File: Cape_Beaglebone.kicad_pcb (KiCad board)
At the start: 2 copper layers, 54.6 x 86.4 mm, 2 parts, among them P8 BeagleBone_Black_Header, P9 BeagleBone_Black_Header

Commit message: mfsb_29_07_18
Primeira tentativa do layout
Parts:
- added C1, C13, C24: 10n, Capacitors_SMD:C_0805, B.Cu at (157.0, 152.6)
- added C10, C11, C12, C29, C9: C, Capacitors_SMD:C_0805, B.Cu at (157.0, 152.6)
- added C14, C16, C20, C3, C4, C5, C7, C8: 0.1u, Capacitors_SMD:C_0805, B.Cu at (157.0, 152.6)
- added C15, C2, C25, C27, C6: 10u, Capacitors_SMD:C_0805, B.Cu at (157.0, 152.6)
- added C17: 22u, Capacitors_SMD:C_0805, B.Cu at (157.0, 152.6)
- added C18, C26: 4.7u, Capacitors_SMD:C_0805, B.Cu at (157.0, 152.6)
- added C19, C22, C23: 100n, Capacitors_SMD:C_0805, B.Cu at (157.0, 152.6)
- added C21: 0.22u, Capacitors_SMD:C_0805, B.Cu at (157.0, 152.6)
- added C28: 1u, Capacitors_SMD:C_0805, B.Cu at (157.0, 152.6)
- added IC1: MPU-9250, MPU-9250:QFN40P300X300X105-25N-D, B.Cu at (103.7, 157.6)
- added IC10: ADS8688IDBT, ADS8688IDBT:SOP50P640X120-38N, B.Cu at (125.3, 139.9)
- added IC2: HX711, HX711:SOIC127P600X160-16N, B.Cu at (113.8, 152.6)
- added IC3: HX711, HX711:SOIC127P600X160-16N, B.Cu at (125.3, 151.9)
- added IC4: CAT24C256WI-GT3, CAT24C256WI-GT3:SOIC127P800X203-8N, B.Cu at (113.8, 138.6)
- added IC5: AD7793BRUZ, AD7793BRUZ:SOP65P640X120-16N, B.Cu at (102.4, 138.6)
- added IC6: AD7793BRUZ, AD7793BRUZ:SOP65P640X120-16N, B.Cu at (91.0, 138.6)
- added IC7: MPU-6500, MPU-6500:QFN40P300X300X95-25N-D, B.Cu at (111.3, 152.6)
- added IC8: HMC5883L-TR, HMC5883L-TR:16-PIN-LPCC, B.Cu at (89.7, 157.6)
- added IC9: BMP180, BMP180:BMP180, B.Cu at (110.0, 146.2)
- added J1: Conn_01x04, Connectors_JST:JST_GH_BM04B-GHS-TBT_04x1.25mm_Straight, F.Cu at (179.2, 80.2)
- added J10: Conn_01x12, Connectors_JST:JST_GH_BM12B-GHS-TBT_12x1.25mm_Straight, F.Cu at (198.9, 81.4)
- added J11: Conn_01x08, Connectors_JST:JST_GH_BM08B-GHS-TBT_08x1.25mm_Straight, F.Cu at (196.4, 110.6)
- added J12: Conn_01x08, Connectors_JST:JST_GH_BM08B-GHS-TBT_08x1.25mm_Straight, F.Cu at (196.4, 120.8)
- added J2: Conn_01x02, Connectors_JST:JST_GH_BM02B-GHS-TBT_02x1.25mm_Straight, F.Cu at (179.9, 71.3)
- added J3: Conn_01x04, Connectors_JST:JST_GH_BM04B-GHS-TBT_04x1.25mm_Straight, F.Cu at (179.2, 89.1)
- added J4: Conn_01x04, Connectors_JST:JST_GH_BM04B-GHS-TBT_04x1.25mm_Straight, F.Cu at (179.2, 97.9)
- added J6: Conn_01x12, Connectors_JST:JST_GH_BM12B-GHS-TBT_12x1.25mm_Straight, F.Cu at (198.9, 72.5)
- added J7: Conn_01x04, Connectors_JST:JST_GH_BM04B-GHS-TBT_04x1.25mm_Straight, F.Cu at (179.2, 106.8)
- added J8: Conn_01x08, Connectors_JST:JST_GH_BM08B-GHS-TBT_08x1.25mm_Straight, F.Cu at (196.4, 91.6)
- added J9: Conn_01x08, Connectors_JST:JST_GH_BM08B-GHS-TBT_08x1.25mm_Straight, F.Cu at (196.4, 100.5)
- added Q1: BC807, TO_SOT_Packages_SMD:SOT-23, B.Cu at (97.3, 146.2)
- added Q2: BC807, TO_SOT_Packages_SMD:SOT-23, B.Cu at (97.3, 152.6)
- added R1, R2, R3: R, Resistors_SMD:R_0805, B.Cu at (157.0, 152.6)
- added R10, R11, R12, R13, R14: 10k, Resistors_SMD:R_0805, B.Cu at (157.0, 152.1)
- added R4, R5, R6: R, Resistors_SMD:R_0805, B.Cu at (157.0, 152.1)
- added R7, R8, R9: 4.7k, Resistors_SMD:R_0805, B.Cu at (157.0, 152.1)
- added U1: DS3231S#, DS3231S#:SOIC127P1032X265-16N, B.Cu at (136.4, 97.4)
- added U2: 4525DO-DS5AI001DP, 4525DO-DS5AI001DP:4525DO-DS...P, F.Cu at (148.9, 125.4)
- added U3: LSM303D, LSM303DLHC:LGA14-3X5X1-14L, B.Cu at (120.2, 144.9)
- added U4: L3GD20, L3GD20TR:L3GD20TR, B.Cu at (103.7, 146.2)
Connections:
- net GNDD renamed -BATT
- net Net-(P8-Pad13) renamed INTERUP_SEN_7a
- net Net-(P8-Pad15) renamed INTERUP_SEN_7b
- P8 pad 10: Net-(P8-Pad10) -> INTERUP_SEN_4
- P8 pad 11: Net-(P8-Pad11) -> INTERUP_SEN_5
- P8 pad 14: Net-(P8-Pad14) -> INTERUP_SEN_8a
- P8 pad 16: Net-(P8-Pad16) -> INTERUP_SEN_8b
- P8 pad 7: Net-(P8-Pad7) -> INTERUP_SEN_1
- P8 pad 8: Net-(P8-Pad8) -> INTERUP_SEN_2
- P9 pad 17: Net-(P9-Pad17) -> SCL_I2C_1
- P9 pad 18: Net-(P9-Pad18) -> SDA_I2C_1
- P9 pad 19: Net-(P9-Pad19) -> SCL_I2C_2
- P9 pad 20: Net-(P9-Pad20) -> SDA_I2C_2
- P9 pad 29: Net-(P9-Pad29) -> SPI_SD0
- P9 pad 30: Net-(P9-Pad30) -> SPI_SDI
- P9 pad 31: Net-(P9-Pad31) -> SPI_SPC
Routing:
- added copper zone on B.Cu, net +3V3
- added copper zone on F.Cu, net GNDD

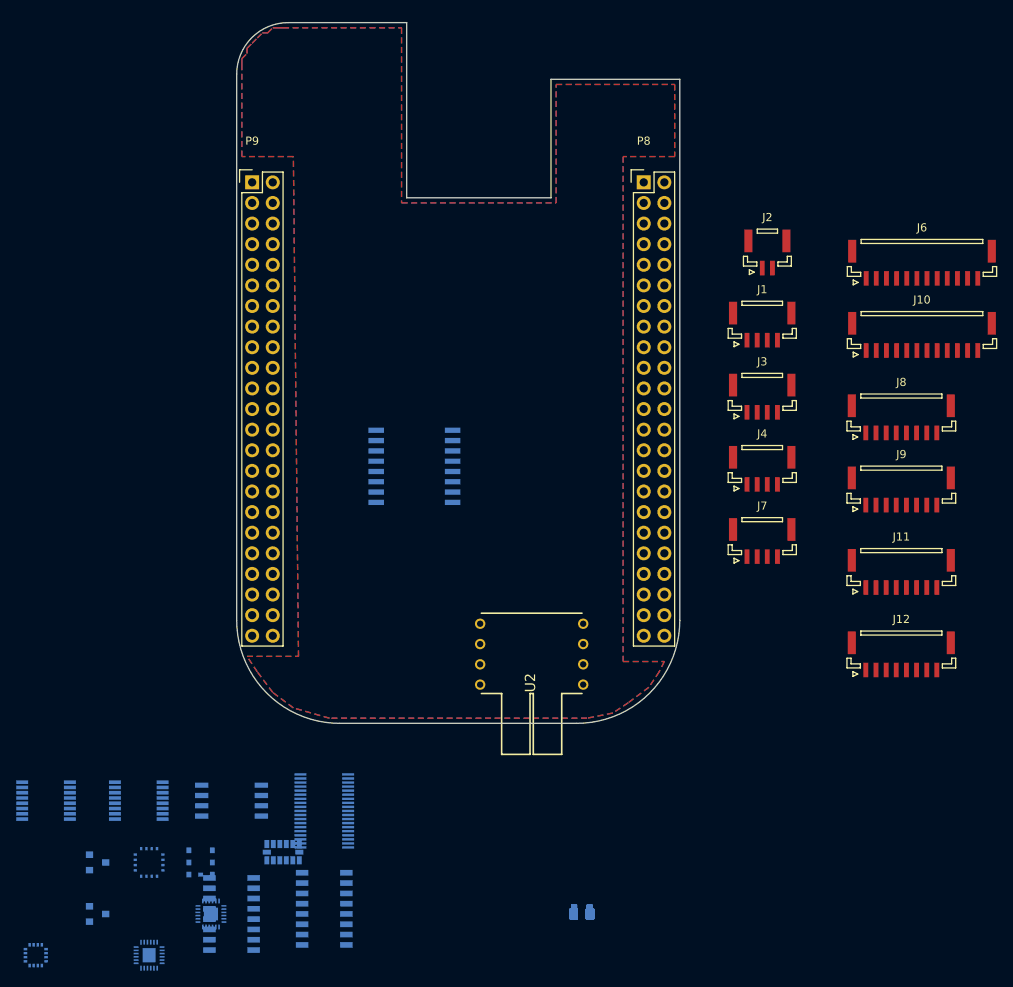
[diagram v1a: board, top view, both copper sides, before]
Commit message: Layout com SJT GH
Layout quase finalizado usando os conectores SJT GH de 1,25 mm
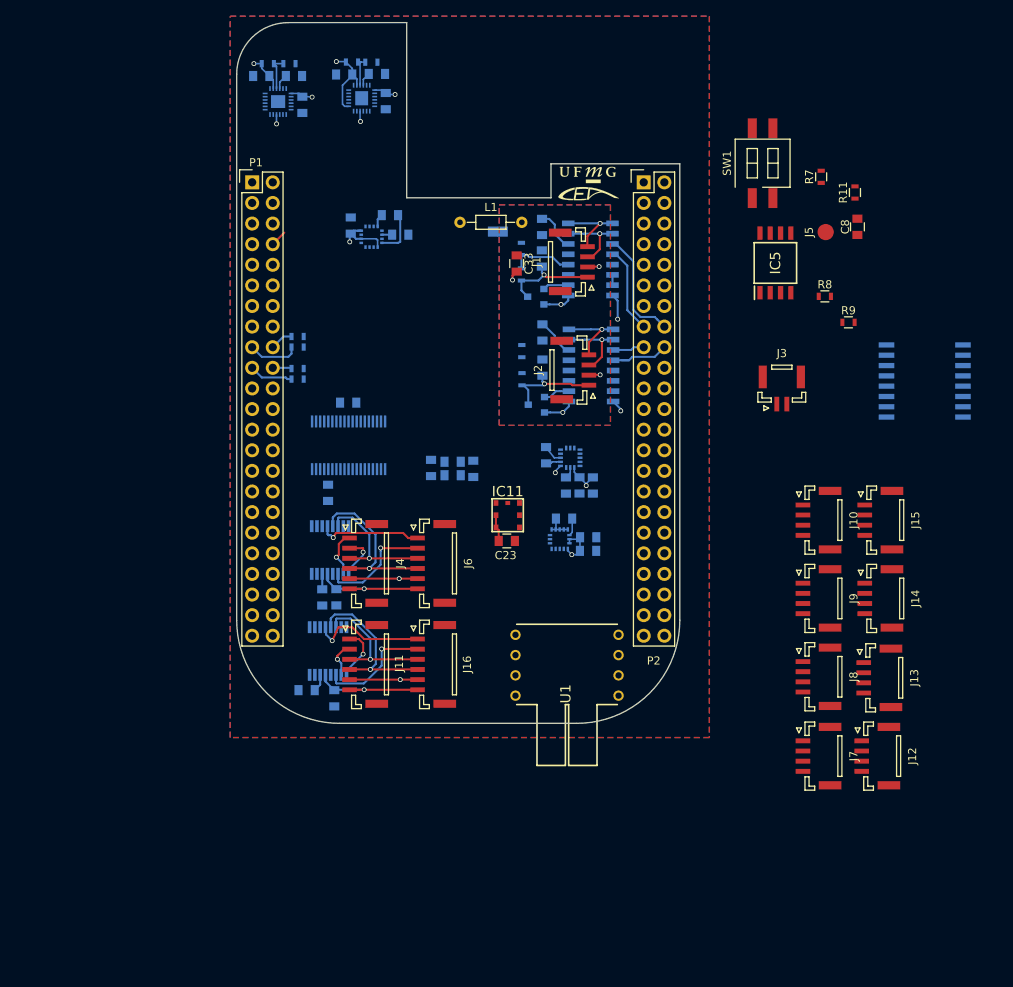
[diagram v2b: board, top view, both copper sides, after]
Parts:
- removed P8, P9: BeagleBone_Black_Header, Socket_BeagleBone_Black:Socket_BeagleBone_Black
- removed U2: 4525DO-DS5AI001DP, 4525DO-DS5AI001DP:4525DO-DS...P
- removed U3: LSM303D, LSM303DLHC:LGA14-3X5X1-14L
- removed U4: L3GD20, L3GD20TR:L3GD20TR
- added C30: 1u, Capacitors_SMD:C_0805, B.Cu at (128.2, 89.5)
- added C31: 10n, Capacitors_SMD:C_0805, B.Cu at (154.8, 103.8)
- added C32: 10u, Capacitors_SMD:C_0805, B.Cu at (157.8, 107.8)
- added C33: C, Capacitors_SMD:C_0805, F.Cu at (149.0, 72.4)
- added G***: UFMG, complementos:UFMG, F.Cu at (157.7, 61.5)
- added G***: CEA, complementos:CEA, F.Cu at (157.8, 63.8)
- added IC11: BMP180, BMP180:BMP180, F.Cu at (147.9, 103.4)
- added IC12: ADS8688IDBT, ADS8688IDBT:SOP50P640X120-38N, B.Cu at (128.3, 94.8)
- added IC13: L3GD20H, L3GD20H_CORRETO:LGA(3X3X1.0-16L), B.Cu at (154.3, 106.4)
- added J13: Conn_01x04, Connectors_JST:JST_GH_BM04B-GHS-TBT_04x1.25mm_Straight, F.Cu at (193.4, 123.4)
- added J14: Conn_01x04, Connectors_JST:JST_GH_BM04B-GHS-TBT_04x1.25mm_Straight, F.Cu at (193.5, 113.7)
- added J15: Conn_01x04, Connectors_JST:JST_GH_BM04B-GHS-TBT_04x1.25mm_Straight, F.Cu at (193.5, 104.0)
- added J16: Conn_01x06, Connectors_JST:JST_GH_BM06B-GHS-TBT_06x1.25mm_Straight, F.Cu at (138.4, 121.8)
- added J5: M_WP, complemento2:test_pad, F.Cu at (184.5, 68.5)
- added L1: I, Resistors_THT:R_Axial_DIN0204_L3.6mm_D1.6mm_P7.62mm_Horizontal, F.Cu at (142.0, 67.3)
- added NT1: Net-Tie_2, complementos:net_tie2, B.Cu at (144.7, 69.7)
- added P1: BeagleBone_Black_Header, Socket_BeagleBone_Black:Socket_BeagleBone_Black, F.Cu at (116.4, 62.4)
- added P2: BeagleBone_Black_Header, Socket_BeagleBone_Black:Socket_BeagleBone_Black, F.Cu at (164.6, 62.4)
- added R15: 10k, Resistors_SMD:R_0603, B.Cu at (122.0, 82.7)
- added R16: 10k, Resistors_SMD:R_0603, B.Cu at (122.0, 81.4)
- added SW1: SW_DIP_x02, Buttons_Switches_SMD:SW_DIP_x2_W8.61mm_Slide_LowProfile, F.Cu at (179.3, 60.0)
- C1: value 10n -> 10u
- C13: value 10n -> C
- C14: value 0.1u -> 10n
- C15: value 10u -> 0.1u
- C17: value 22u -> 4.7u
- C18: value 4.7u -> 10u
- C19: value 100n -> 0.1u
- C2: value 10u -> 10n
- C20: value 0.1u -> 1u
- C23, C8: moved to F.Cu
- C24: value 10n -> 22u
- C26: value 4.7u -> 1u
- C27: value 10u -> 4.7u
- C28: value 1u -> 100n
- C29: value C -> 10u
- C9: value C -> 22u
- IC10: value ADS8688IDBT -> HMC5883L-TR; footprint ADS8688IDBT:SOP50P640X120-38N -> HMC5883L-TR:16-PIN-LPCC
- IC3: value HX711 -> DS3231S; footprint HX711:SOIC127P600X160-16N -> DS3231S#:SOIC127P1032X265-16N
- IC4: value CAT24C256WI-GT3 -> HX711; footprint CAT24C256WI-GT3:SOIC127P800X203-8N -> HX711:SOIC127P600X160-16N
- IC5: value AD7793BRUZ -> CAT24C256WI-GT3; footprint AD7793BRUZ:SOP65P640X120-16N -> CAT24C256WI-GT3:SOIC127P800X203-8N; moved to F.Cu
- IC7: value MPU-6500 -> AD7793BRUZ; footprint MPU-6500:QFN40P300X300X95-25N-D -> AD7793BRUZ:SOP65P640X120-16N
- IC8: value HMC5883L-TR -> MPU-6500; footprint HMC5883L-TR:16-PIN-LPCC -> MPU-6500:QFN40P300X300X95-25N-D
- IC9: value BMP180 -> LSM303D; footprint BMP180:BMP180 -> LSM303D:PQFN50P300X300X100-16N
- J10: value Conn_01x12 -> Conn_01x04; footprint Connectors_JST:JST_GH_BM12B-GHS-TBT_12x1.25mm_Straight -> Connectors_JST:JST_GH_BM04B-GHS-TBT_04x1.25mm_Straight
- J11: value Conn_01x08 -> Conn_01x06; footprint Connectors_JST:JST_GH_BM08B-GHS-TBT_08x1.25mm_Straight -> Connectors_JST:JST_GH_BM06B-GHS-TBT_06x1.25mm_Straight
- J12, J8, J9: value Conn_01x08 -> Conn_01x04; footprint Connectors_JST:JST_GH_BM08B-GHS-TBT_08x1.25mm_Straight -> Connectors_JST:JST_GH_BM04B-GHS-TBT_04x1.25mm_Straight
- J2: value Conn_01x02 -> Conn_01x04; footprint Connectors_JST:JST_GH_BM02B-GHS-TBT_02x1.25mm_Straight -> Connectors_JST:JST_GH_BM04B-GHS-TBT_04x1.25mm_Straight
- J3: value Conn_01x04 -> Conn_01x02; footprint Connectors_JST:JST_GH_BM04B-GHS-TBT_04x1.25mm_Straight -> Connectors_JST:JST_GH_BM02B-GHS-TBT_02x1.25mm_Straight
- J4: value Conn_01x04 -> Conn_01x06; footprint Connectors_JST:JST_GH_BM04B-GHS-TBT_04x1.25mm_Straight -> Connectors_JST:JST_GH_BM06B-GHS-TBT_06x1.25mm_Straight
- J6: value Conn_01x12 -> Conn_01x06; footprint Connectors_JST:JST_GH_BM12B-GHS-TBT_12x1.25mm_Straight -> Connectors_JST:JST_GH_BM06B-GHS-TBT_06x1.25mm_Straight
- R1, R10, R12, R2, R3, R4, R5, R6: footprint Resistors_SMD:R_0805 -> Resistors_SMD:R_0603
- R11, R7, R8, R9: footprint Resistors_SMD:R_0805 -> Resistors_SMD:R_0603; moved to F.Cu
- R13, R14: value 10k -> R; footprint Resistors_SMD:R_0805 -> Resistors_SMD:R_0603
- U1: value DS3231S# -> 4525DO-DS5AI001DP; footprint DS3231S#:SOIC127P1032X265-16N -> 4525DO-DS5AI001DP:4525DO-DS...P; moved to F.Cu
- moved R13 111.3 mm to (118.3, 47.8), turned to 180 degrees
- moved C14 110.6 mm to (117.5, 49.3), turned to 180 degrees
- moved R14 110.4 mm to (121.0, 47.8), turned to 180 degrees
- moved IC8 109.4 mm to (119.6, 52.4)
- moved C15 109.2 mm to (121.5, 49.3), turned to 180 degrees
- moved IC1 108.8 mm to (129.9, 52.0)
- moved R3 108.7 mm to (128.7, 47.6), turned to 180 degrees
- moved R4 107.7 mm to (131.1, 47.6), turned to 180 degrees
- moved C2 107.5 mm to (127.7, 49.1), turned to 180 degrees
- moved C4 106.6 mm to (131.7, 49.0), turned to 180 degrees
- moved C16 105.5 mm to (122.6, 52.8), turned to 270 degrees
- moved C5 103.1 mm to (132.8, 52.4), turned to 270 degrees
- moved IC5 102.7 mm to (180.9, 72.3), turned to 90 degrees
- moved IC3 98.5 mm to (199.3, 86.9), turned to 180 degrees
- moved R7 95.1 mm to (186.5, 61.7), turned to 90 degrees
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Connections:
- C1 pad 1: +3V3 -> GNDA
- C1 pad 2: -BATT -> Net-(C1-Pad2)
- C10 pad 1: +5VA -> GNDD
- C10 pad 2: GNDA -> +3V3
- C11 pad 1: GND -> +5VA
- C11 pad 2: +3V3 -> GNDA
- C12 pad 1: +5VA -> GNDD
- C12 pad 2: GNDA -> +3V3
- C13 pad 1: +3V3 -> +5VA
- C13 pad 2: -BATT -> GNDA
- C14 pad 1: Net-(C14-Pad1) -> +3V3
- C14 pad 2: -BATT -> GNDD
- C15 pad 1: +3V3 -> GNDD
- C15 pad 2: -BATT -> Net-(C15-Pad2)
- C16 pad 2: -BATT -> GNDD
- C17 pad 2: Net-(C17-Pad2) -> GNDD
- C18 pad 1: Net-(C18-Pad1) -> +3V3
- C18 pad 2: -BATT -> GNDD
- C19 pad 2: -BATT -> GNDD
- C2 pad 1: GNDA -> +3V3
- C2 pad 2: +5VA -> GNDD
- C20 pad 1: +3V3 -> +5VA
- C20 pad 2: -BATT -> GNDA
- C22 pad 2: Net-(C22-Pad2) -> GNDD
- C23 pad 2: -BATT -> GNDD
- C24 pad 2: -BATT -> GNDA
- C25 pad 1: +3V3 -> GNDA
- C25 pad 2: -BATT -> Net-(C25-Pad2)
- C26 pad 1: -BATT -> Net-(C24-Pad1)
- C26 pad 2: Net-(C26-Pad2) -> GNDA
- C27 pad 1: +3V3 -> GNDD
- C27 pad 2: -BATT -> Net-(C27-Pad2)
- C28 pad 1: GNDA -> +3V3
- C28 pad 2: +5VA -> GNDD
- C29 pad 1: +5VA -> +3V3
- C29 pad 2: GNDA -> GNDD
- C4 pad 1: -BATT -> GNDD
- C5 pad 2: -BATT -> GNDD
- C6 pad 2: +5VA -> Net-(C6-Pad2)
- C8 pad 2: -BATT -> GNDD
- C9 pad 1: GND -> Net-(C9-Pad1)
- C9 pad 2: +3V3 -> Net-(C9-Pad2)
- IC1 pad 12: INTERUP_SEN_4 -> INTERUP_SEN_3
- IC1 pad 18: -BATT -> GNDD
- IC1 pad 20: -BATT -> GNDD
- IC1 pad 25: Net-(IC1-Pad25) -> GNDD
- IC10 pad 1: SPI_SDI -> SCL_I2C_1
- IC10 pad 10: Net-(IC10-Pad10) -> Net-(C27-Pad2)
- IC10 pad 11: Net-(IC10-Pad11) -> GNDD
- IC10 pad 12: /AIN_6P -> Net-(C21-Pad2)
- IC10 pad 13: /AIN_6N -> +3V3
- IC10 pad 14: /AIN_7P -> Net-(IC10-Pad14)
- IC10 pad 15: /AIN_7N -> INTERUP_SEN_2
- IC10 pad 16: /AIN_0P -> SDA_I2C_1
- IC10 pad 2: Net-(IC10-Pad2) -> +3V3
- IC10 pad 4: Net-(IC10-Pad4) -> +3V3
- IC10 pad 8: GNDA -> Net-(C21-Pad1)
- IC10 pad 9: +5VA -> GNDD
- IC2 pad 1: Net-(IC2-Pad1) -> +5VA
- IC2 pad 11: Net-(IC2-Pad11) -> HX1_SCK
- IC2 pad 12: Net-(IC2-Pad12) -> HX1_DOUT
- IC2 pad 14: -BATT -> GNDD
- IC2 pad 15: -BATT -> GNDD
- IC2 pad 7: Net-(IC2-Pad7) -> Net-(IC2-Pad10)
- IC2 pad 9: Net-(IC2-Pad9) -> Net-(IC2-Pad8)
- IC3 pad 10: Net-(IC3-Pad10) -> GNDD
- IC3 pad 11: Net-(IC3-Pad11) -> GNDD
- IC3 pad 12: Net-(IC3-Pad12) -> GNDD
- IC3 pad 13: Net-(IC3-Pad13) -> GNDD
- IC3 pad 14: -BATT -> Net-(IC3-Pad14)
- IC3 pad 15: -BATT -> SDA_I2C_2
- IC3 pad 16: +3V3 -> SCL_I2C_2
- IC3 pad 2: Net-(IC3-Pad2) -> +3V3
- IC3 pad 3: +5VA -> INTERUP_RTC
- IC3 pad 5: GNDA -> GNDD
- IC3 pad 6: Net-(C7-Pad1) -> GNDD
- IC3 pad 7: Net-(IC3-Pad7) -> GNDD
- IC3 pad 8: Net-(IC3-Pad8) -> GNDD
- IC3 pad 9: Net-(IC3-Pad9) -> GNDD
- IC4 pad 1: Net-(IC4-Pad1) -> +5VA
- IC4 pad 3: Net-(IC4-Pad3) -> +5VA
- IC4 pad 4: -BATT -> Net-(IC4-Pad4)
- IC4 pad 5: SDA_I2C_2 -> GNDA
- IC4 pad 6: SCL_I2C_2 -> Net-(C7-Pad1)
- IC4 pad 7: Net-(IC4-Pad7) -> Net-(IC4-Pad10)
- IC4 pad 8: +3V3 -> Net-(IC4-Pad8)
- IC5 pad 1: SPI_SPC -> Net-(IC5-Pad1)
- IC5 pad 3: SPI_CS_S1 -> Net-(IC5-Pad3)
- IC5 pad 4: Net-(IC5-Pad4) -> GNDD
- IC5 pad 5: /AIN_8P -> SDA_I2C_2
- IC5 pad 6: /AIN_8N -> SCL_I2C_2
- IC5 pad 7: /AIN_9P -> Net-(IC5-Pad7)
- IC5 pad 8: /AIN_9N -> +3V3
- IC6 pad 11: Net-(IC6-Pad11) -> /IOUT_4
- IC6 pad 4: Net-(IC6-Pad4) -> /IOUT_3
- IC6 pad 7: /AIN_12P -> Net-(IC6-Pad7)
- IC6 pad 8: /AIN_12N -> Net-(IC6-Pad8)
- IC7 pad 1: Net-(IC7-Pad1) -> SPI_SPC
- IC7 pad 10: Net-(C14-Pad1) -> /AIN_9P
- IC7 pad 11: Net-(IC7-Pad11) -> /IOUT_2
- IC7 pad 12: INTERUP_SEN_1 -> GNDA
- IC7 pad 13: +3V3 -> +5VA
- IC7 pad 14: Net-(IC7-Pad14) -> +3V3
- IC7 pad 15: Net-(IC7-Pad15) -> SPI_SD0
- IC7 pad 16: Net-(IC7-Pad16) -> SPI_SDI
- IC7 pad 3: Net-(IC7-Pad3) -> SPI_CS_S1
- IC7 pad 4: Net-(IC7-Pad4) -> /IOUT_1
- IC7 pad 5: Net-(IC7-Pad5) -> /AIN_8P
- IC7 pad 6: Net-(IC7-Pad6) -> /AIN_8N
- IC7 pad 8: +3V3 -> Net-(IC7-Pad8)
- IC7 pad 9: Net-(IC7-Pad9) -> /AIN_9N
- IC8 pad 1: SCL_I2C_1 -> Net-(IC8-Pad1)
- IC8 pad 10: Net-(C26-Pad2) -> Net-(C15-Pad2)
- IC8 pad 11: -BATT -> Net-(IC8-Pad11)
- IC8 pad 12: Net-(C21-Pad2) -> INTERUP_SEN_1
- IC8 pad 15: INTERUP_SEN_2 -> Net-(IC8-Pad15)
- IC8 pad 16: SDA_I2C_1 -> Net-(IC8-Pad16)
- IC8 pad 2: +3V3 -> Net-(IC8-Pad2)
- IC8 pad 4: +3V3 -> Net-(IC8-Pad4)
- IC8 pad 8: Net-(C21-Pad1) -> +3V3
- IC8 pad 9: -BATT -> Net-(IC8-Pad9)
- IC9 pad 1: Net-(IC9-Pad1) -> +3V3
- IC9 pad 2: +3V3 -> Net-(C9-Pad1)
- IC9 pad 3: +3V3 -> Net-(C9-Pad2)
- IC9 pad 4: Net-(IC9-Pad4) -> SPI_SPC
- IC9 pad 5: SCL_I2C_1 -> GNDD
- IC9 pad 6: SDA_I2C_1 -> SPI_SDI
- IC9 pad 7: -BATT -> SPI_SD0
- J1 pad 1: +5VA -> Net-(C1-Pad2)
- J1 pad 3: Net-(IC2-Pad8) -> Net-(IC2-Pad10)
- J1 pad 4: Net-(IC2-Pad7) -> Net-(IC2-Pad8)
- J10 pad 1: /AIN_11P -> GNDA
- J10 pad 2: /AIN_11N -> +5VA
- J10 pad 3: +5VA -> /AIN_1P
- J10 pad 4: GNDA -> /AIN_1N
- J11 pad 1: /AIN_4N -> /AIN_13P
- J11 pad 2: /AIN_4P -> /AIN_13N
- J11 pad 3: +5VA -> /AIN_11N
- J11 pad 4: GNDA -> /AIN_11P
- J11 pad 5: /AIN_5N -> GNDA
- J11 pad 6: /AIN_5P -> +5VA
- J12 pad 1: /AIN_2N -> GNDA
- J12 pad 2: /AIN_2P -> +5VA
- J12 pad 3: +5VA -> /AIN_5P
- J12 pad 4: GNDA -> /AIN_5N
- J2 pad 1: -BATT -> Net-(C6-Pad2)
- J2 pad 2: +BATT -> GNDA
- J3 pad 1: +5VA -> Net-(IC3-Pad14)
- J3 pad 2: GNDA -> GNDD
- J4 pad 1: +5VA -> /AIN_9P
- J4 pad 2: GNDA -> /AIN_9N
- J4 pad 3: Net-(IC3-Pad8) -> /AIN_8N
- J4 pad 4: Net-(IC3-Pad7) -> /AIN_8P
- J6 pad 1: /AIN_8P -> /IOUT_1
- J6 pad 2: /AIN_8N -> /IOUT_2
- J6 pad 3: +5VA -> /AIN_8N
- J6 pad 4: GNDA -> /AIN_8P
- J6 pad 5: /AIN_9P -> GNDA
- J6 pad 6: /AIN_9N -> +5VA
- J7 pad 1: +5VA -> GNDA
- J7 pad 2: GNDA -> +5VA
- J7 pad 3: Net-(IC3-Pad9) -> /AIN_6P
- J7 pad 4: Net-(IC3-Pad10) -> /AIN_6N
- J8 pad 1: /AIN_7N -> GNDA
- J8 pad 2: /AIN_7P -> +5VA
- J8 pad 3: +5VA -> /AIN_7P
- J8 pad 4: GNDA -> /AIN_7N
- J9 pad 1: /AIN_1N -> GNDA
- J9 pad 2: /AIN_1P -> +5VA
- J9 pad 3: +5VA -> /AIN_0P
- J9 pad 4: GNDA -> /AIN_0N
- Q1 pad 2: Net-(IC2-Pad1) -> +5VA
- Q1 pad 3: +5VA -> Net-(C1-Pad2)
- Q2 pad 1: Net-(IC3-Pad2) -> Net-(IC4-Pad2)
- Q2 pad 2: Net-(IC3-Pad1) -> +5VA
- Q2 pad 3: +5VA -> Net-(C6-Pad2)
- R1 pad 1: Net-(IC1-Pad9) -> Net-(IC2-Pad4)
- R1 pad 2: +3V3 -> Net-(C1-Pad2)
- R11 pad 2: Net-(IC4-Pad7) -> Net-(IC5-Pad7)
- R13 pad 1: SCL_I2C_1 -> Net-(IC8-Pad9)
- R14 pad 1: SDA_I2C_1 -> GNDD
- R14 pad 2: +3V3 -> Net-(IC8-Pad9)
- R2 pad 1: +5VA -> GNDA
- R3 pad 1: Net-(IC2-Pad4) -> Net-(IC1-Pad9)
- R3 pad 2: GNDA -> +3V3
- R4 pad 1: -BATT -> GNDD
- R5 pad 1: +5VA -> Net-(IC4-Pad4)
- R5 pad 2: Net-(IC3-Pad4) -> Net-(C6-Pad2)
- R6 pad 1: Net-(IC3-Pad4) -> GNDA
- R6 pad 2: GNDA -> Net-(IC4-Pad4)
- R7 pad 2: Net-(IC4-Pad1) -> Net-(IC5-Pad1)
- R8 pad 2: Net-(IC4-Pad2) -> Net-(IC5-Pad2)
- R9 pad 2: Net-(IC4-Pad3) -> Net-(IC5-Pad3)
- U1 pad 1: Net-(U1-Pad1) -> GNDD
- U1 pad 3: Net-(U1-Pad3) -> SDA_I2C_2
- U1 pad 4: Net-(SW1-Pad4) -> SCL_I2C_2
- U1 pad 5: -BATT -> INTERUP_SEN_4
- U1 pad 6: -BATT -> Net-(U1-Pad6)
- U1 pad 7: -BATT -> Net-(U1-Pad7)
- U1 pad 8: -BATT -> Net-(U1-Pad8)
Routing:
- net +3V3: track 0.00 -> 53.3 mm, vias 0 -> 12
- net +5VA: track 0.00 -> 36.3 mm, vias 0 -> 4
- net GNDA: track 0.00 -> 20.9 mm, vias 0 -> 5
- net /AIN_11P: track 0.00 -> 20.6 mm, vias 0 -> 1
- net /AIN_8P: track 0.00 -> 20.5 mm, vias 0 -> 1
- net /AIN_11N: track 0.00 -> 17.2 mm, vias 0 -> 1
- net /AIN_8N: track 0.00 -> 17.1 mm, vias 0 -> 1
- net /IOUT_3: track 0.00 -> 14.2 mm, vias 0 -> 1
- net HX1_SCK: track 0.00 -> 14.1 mm
- net /IOUT_4: track 0.00 -> 14.0 mm, vias 0 -> 1
- net /IOUT_2: track 0.00 -> 13.8 mm, vias 0 -> 1
- net /IOUT_1: track 0.00 -> 12.9 mm, vias 0 -> 1
- net Net-(C6-Pad2): track 0.00 -> 12.3 mm, vias 0 -> 1
- net Net-(C1-Pad2): track 0.00 -> 12.0 mm, vias 0 -> 1
- net HX1_DOUT: track 0.00 -> 10.8 mm
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- added copper zone on F.Cu, net +3V3
- added copper zone on F.Cu, net +5VA
- added copper zone on B.Cu, net GNDA
- added copper zone on B.Cu, net GNDD
- removed copper zone on B.Cu, net +3V3
- removed copper zone on F.Cu, net GNDD
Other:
- outline, holes or cut-outs redrawn
- net class fina added: clearance 0.15, trace_width 0.2, via_dia 0.6, via_drill 0.4

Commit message: Final V1.0
Primeria versão final sem revisão
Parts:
- removed the G*** at (157.7, 61.5)
- removed the G*** at (157.8, 63.8)
- added C34: C, Capacitors_SMD:C_0805, F.Cu at (138.5, 67.4)
- added G***: LOGO, complementos:LOGO, F.Cu at (122.0, 91.0)
- added L2: I, Resistors_THT:R_Axial_DIN0204_L3.6mm_D1.6mm_P7.62mm_Horizontal, F.Cu at (133.5, 74.6)
- added NT2: Net-Tie_2, complementos:net_tie2, B.Cu at (136.2, 71.4)
- added R17: 0, Resistors_SMD:R_0603, F.Cu at (166.7, 57.9)
- added R18: 0, Resistors_SMD:R_0603, F.Cu at (165.5, 57.9)
- C17, C18, C22, C9, IC9, R10, R12, R15, R16: moved to F.Cu
- J1, J10, J12, J13, J14, J15, J2, J7, J8, J9: footprint Connectors_JST:JST_GH_BM04B-GHS-TBT_04x1.25mm_Straight -> Connectors_JST:JST_SH_BM04B-SRSS-TB_04x1.00mm_Straight
- J11, J16, J4, J6: footprint Connectors_JST:JST_GH_BM06B-GHS-TBT_06x1.25mm_Straight -> Connectors_JST:JST_SH_BM06B-SRSS-TB_06x1.00mm_Straight
- J3: footprint Connectors_JST:JST_GH_BM02B-GHS-TBT_02x1.25mm_Straight -> Connectors_JST:JST_SH_BM02B-SRSS-TB_02x1.00mm_Straight
- SW1: footprint Buttons_Switches_SMD:SW_DIP_x2_W8.61mm_Slide_LowProfile -> Buttons_Switches_SMD:SW_DIP_x2_W5.08mm_Slide_Copal_CHS-A
- moved C10 75.3 mm to (191.3, 93.2), turned to 90 degrees
- moved C11 75.0 mm to (192.0, 89.6), turned to 90 degrees
- moved U1 72.1 mm to (187.8, 63.4), turned to 180 degrees
- moved IC6 67.6 mm to (186.5, 90.5), turned to 0 degrees
- moved J11 65.2 mm to (184.3, 85.6), turned to 90 degrees
- moved J4 63.9 mm to (184.3, 75.5), turned to 90 degrees
- moved J16 62.9 mm to (189.9, 85.6), turned to 90 degrees
- moved J6 61.6 mm to (189.9, 75.5), turned to 90 degrees
- moved C13 59.9 mm to (181.4, 89.1), turned to 90 degrees
- moved J7 59.2 mm to (152.0, 84.7), turned to 180 degrees
- moved C12 59.1 mm to (180.6, 93.6)
- moved J8 55.8 mm to (152.0, 79.1), turned to 180 degrees
- moved IC7 52.2 mm to (175.3, 90.5), turned to 0 degrees
- moved J12 51.4 mm to (176.1, 84.6), turned to 180 degrees
- moved R13 49.4 mm to (118.5, 97.1), turned to 270 degrees
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- renumbered P1 to P8, P2 to P9
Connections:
- net Net-(P1-Pad32) renamed VDD_ADC
- net Net-(P1-Pad34) renamed GNDA_ADC
- C1 pad 1: GNDA -> GNDA_aux
- C3 pad 2: GNDA -> GNDA_aux
- C6 pad 1: GNDA -> GNDA_aux
- C7 pad 2: GNDA -> GNDA_aux
- IC2 pad 1: +5VA -> +5VA_aux
- IC2 pad 3: +5VA -> +5VA_aux
- IC2 pad 5: GNDA -> GNDA_aux
- IC4 pad 1: +5VA -> +5VA_aux
- IC4 pad 3: +5VA -> +5VA_aux
- IC4 pad 5: GNDA -> GNDA_aux
- J1 pad 2: GNDA -> GNDA_aux
- J11 pad 3: /AIN_11N -> /AIN_11P
- J11 pad 4: /AIN_11P -> /AIN_11N
- J16 pad 1: /IOUT_3 -> /IOUT_4
- J16 pad 2: /IOUT_4 -> /IOUT_3
- J16 pad 3: /AIN_11N -> /AIN_11P
- J16 pad 4: /AIN_11P -> /AIN_11N
- J2 pad 2: GNDA -> GNDA_aux
- J4 pad 3: /AIN_8N -> /AIN_8P
- J4 pad 4: /AIN_8P -> /AIN_8N
- J6 pad 1: /IOUT_1 -> /IOUT_2
- J6 pad 2: /IOUT_2 -> /IOUT_1
- J6 pad 3: /AIN_8N -> /AIN_8P
- J6 pad 4: /AIN_8P -> /AIN_8N
- L1 pad 1: SYS_5V -> +5V
- P8 pad 10: Net-(P1-Pad10) -> INTERUP_SEN_7b
- P8 pad 11: Net-(P1-Pad11) -> SPI_CS_S5
- P8 pad 14: Net-(P1-Pad14) -> SPI_CS_S4
- P8 pad 15: Net-(P1-Pad15) -> INTERUP_SEN_8b
- P8 pad 16: Net-(P1-Pad16) -> INTERUP_SEN_8a
- P8 pad 23: INTERUP_RTC -> Net-(P1-Pad23)
- P8 pad 28: Net-(P1-Pad28) -> SPI_CS_S3
- P8 pad 36: Net-(P1-Pad36) -> SPI_CS_S1
- P8 pad 42: Net-(P1-Pad42) -> SPI_CS_S2
- P8 pad 5: Net-(P1-Pad5) -> +5V
- P8 pad 6: Net-(P1-Pad6) -> +5V
- P8 pad 7: SYS_5V -> INTERUP_SEN_1
- P8 pad 8: SYS_5V -> INTERUP_SEN_2
- P8 pad 9: Net-(P1-Pad9) -> INTERUP_SEN_7a
- P9 pad 10: INTERUP_SEN_4 -> Net-(P2-Pad10)
- P9 pad 11: INTERUP_SEN_7a -> Net-(P2-Pad11)
- P9 pad 12: INTERUP_SEN_8a -> Net-(P2-Pad12)
- P9 pad 13: INTERUP_SEN_7b -> Net-(P2-Pad13)
- P9 pad 14: INTERUP_SEN_8b -> Net-(P2-Pad14)
- P9 pad 27: SPI_CS_S1 -> Net-(P2-Pad27)
- P9 pad 28: SPI_CS_S2 -> Net-(P2-Pad28)
- P9 pad 29: SPI_CS_S3 -> Net-(P2-Pad29)
- P9 pad 30: SPI_CS_S4 -> Net-(P2-Pad30)
- P9 pad 31: SPI_CS_S5 -> Net-(P2-Pad31)
- P9 pad 41: Net-(P2-Pad41) -> INTERUP_SEN_3
- P9 pad 43: Net-(P2-Pad43) -> INTERUP_SEN_4
- P9 pad 44: Net-(P2-Pad44) -> INTERUP_RTC
- P9 pad 7: INTERUP_SEN_1 -> Net-(P2-Pad7)
- P9 pad 8: INTERUP_SEN_2 -> Net-(P2-Pad8)
- P9 pad 9: INTERUP_SEN_3 -> Net-(P2-Pad9)
- Q1 pad 2: +5VA -> +5VA_aux
- Q2 pad 2: +5VA -> +5VA_aux
- R2 pad 1: GNDA -> GNDA_aux
- R6 pad 1: GNDA -> GNDA_aux
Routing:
- net SDA_I2C_2: track 2.35 -> 124.1 mm, vias 0 -> 1
- net SCL_I2C_2: track 5.43 -> 126.1 mm, vias 0 -> 1
- net SPI_SPC: track 0.00 -> 80.1 mm, vias 0 -> 3
- net SPI_SD0: track 0.00 -> 75.8 mm, vias 0 -> 7
- net SPI_SDI: track 0.00 -> 68.9 mm, vias 0 -> 3
- net GNDD: track 1.27 -> 40.2 mm, vias 0 -> 8
- net SDA_I2C_1: track 2.86 -> 39.5 mm, vias 0 -> 1
- net SCL_I2C_1: track 6.33 -> 39.6 mm, vias 0 -> 1
- net INTERUP_RTC: track 0.00 -> 31.5 mm
- net +5V: track 0.00 -> 29.3 mm
- net INTERUP_SEN_1: track 0.00 -> 20.3 mm, vias 0 -> 1
- net INTERUP_SEN_2: track 0.00 -> 19.7 mm, vias 0 -> 2
- net INTERUP_SEN_8b: track 0.00 -> 18.5 mm, vias 0 -> 1
- net INTERUP_SEN_4: track 0.00 -> 17.9 mm
- net INTERUP_SEN_8a: track 0.00 -> 17.6 mm, vias 0 -> 1
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- added copper zone on F.Cu, net +5VA_aux
- added copper zone on B.Cu, net GNDA_aux
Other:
- board size 54.6 x 86.4 mm -> 79.4 x 54.6 mm
- net class fina: clearance 0.15 -> 0.2
- rule via_min_drill: 0.3 -> 0.4
- board text added: "Cape FDAU V1.0 2018"
